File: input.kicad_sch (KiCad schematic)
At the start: 21 parts, among them J1 AV_MULTI_OUT

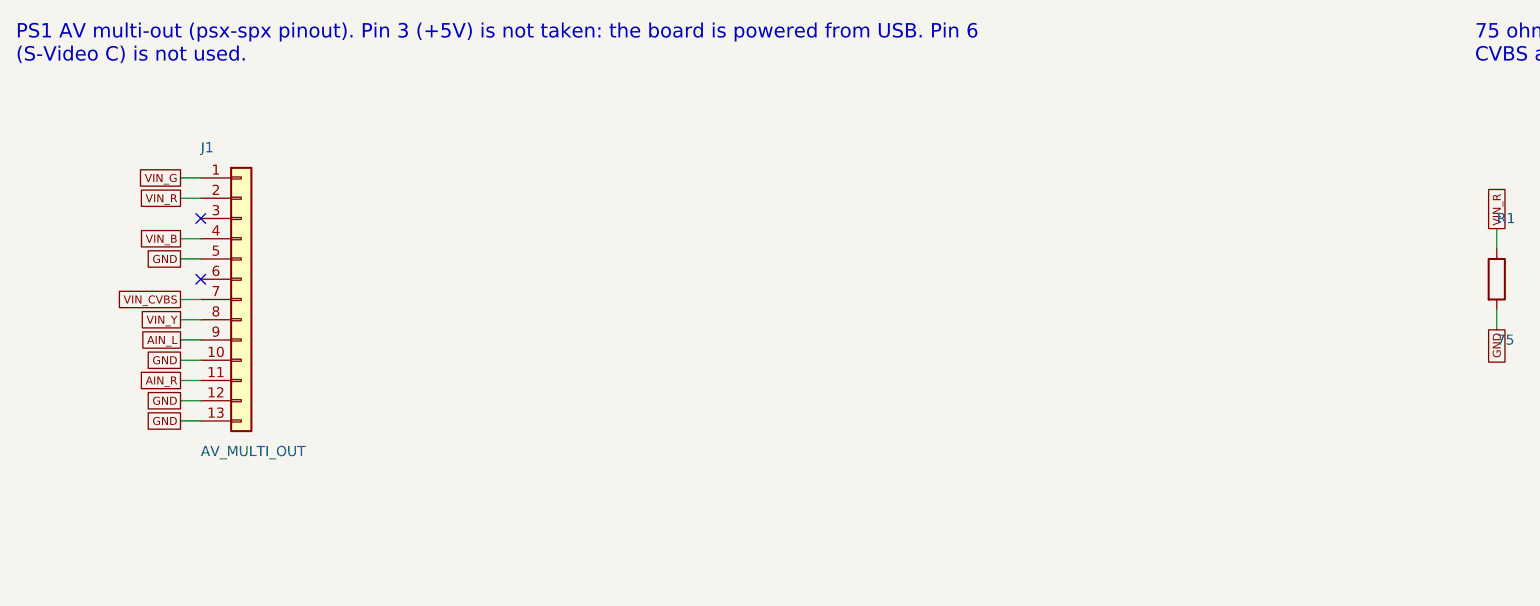
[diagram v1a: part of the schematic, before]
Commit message: J1: JST PHD 2x7 latching header for a multi-AV pigtail, hand-soldered
Signals paired with grounds in each column, DNP in the JLC assembly.
Pigtail pinout and build steps in docs/design.md, hand-built items in docs/parts.md.
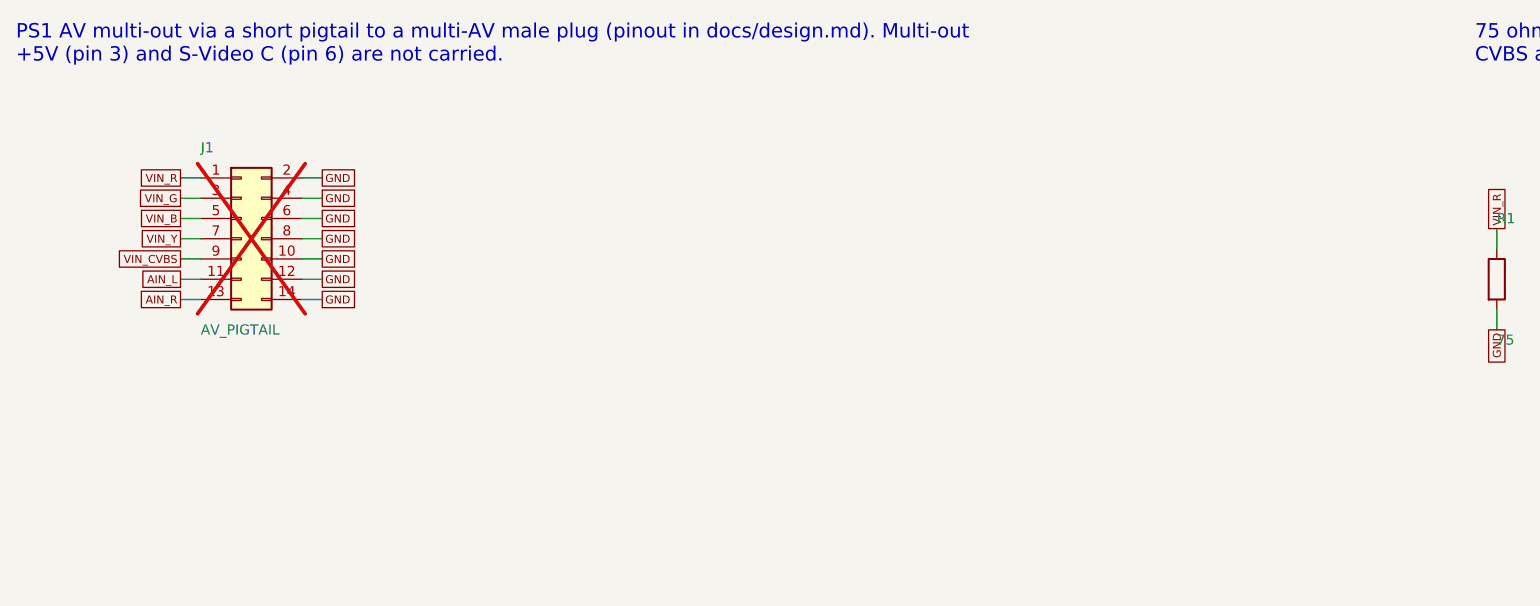
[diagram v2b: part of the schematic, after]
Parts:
- removed J1: AV_MULTI_OUT, Connector_PinHeader_2.54mm:PinHeader_1x13_P2.54mm_Vertical, symbol Connector_Generic:Conn_01x13
- added J1: AV_PIGTAIL, Connector_JST:JST_PHD_B14B-PHDSS_2x07_P2.00mm_Vertical, symbol Connector_Generic:Conn_02x07_Odd_Even
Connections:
- net AIN_L: now also J1.11 (Pin_11)
- net AIN_R: now also J1.13 (Pin_13)
- net GND: now also J1.10 (Pin_10), J1.12 (Pin_12), J1.14 (Pin_14), J1.2 (Pin_2), J1.4 (Pin_4), J1.6 (Pin_6), J1.8 (Pin_8)
- net VIN_B: now also J1.5 (Pin_5)
- net VIN_CVBS: now also J1.9 (Pin_9)
- net VIN_G: now also J1.3 (Pin_3)
- net VIN_R: now also J1.1 (Pin_1)
- net VIN_Y: now also J1.7 (Pin_7)
- no-connect marks 11 -> 9
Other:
- note added: "PS1 AV multi-out via a short pigtail to a multi-AV male plug (pinout in docs/design.md). Multi-out +5V (pin 3) and S-Video C (pin 6) are not carried."
- note removed: "PS1 AV multi-out (psx-spx pinout). Pin 3 (+5V) is not taken: the board is powered from USB. Pin 6 (S-Video C) is not used."
